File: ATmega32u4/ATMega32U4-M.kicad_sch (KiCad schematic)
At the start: 19 parts, among them U2 ATmega32U4-M, Y1 16MHz

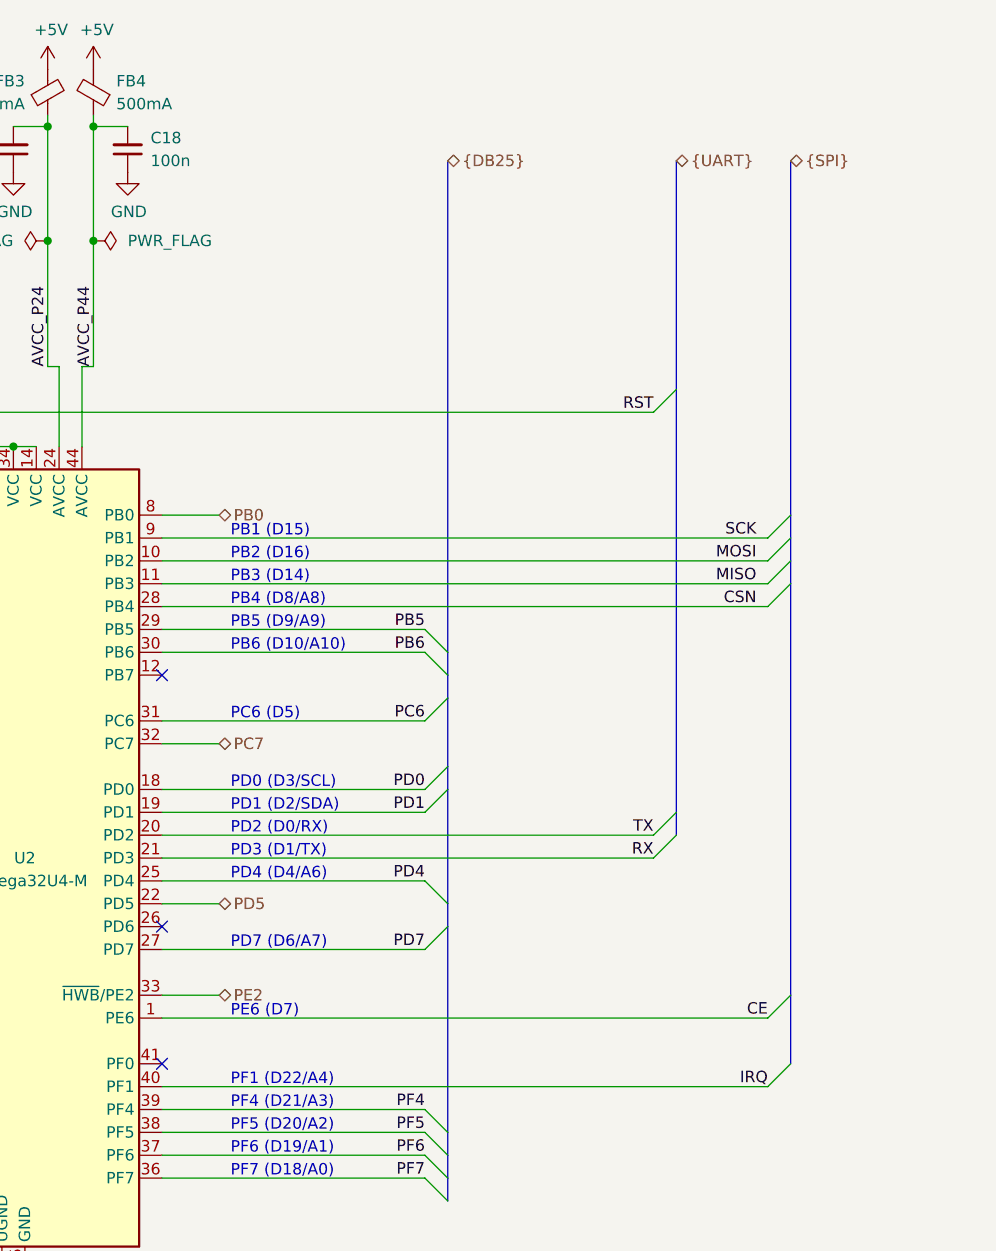
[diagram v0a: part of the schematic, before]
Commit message: Review and updates to power path
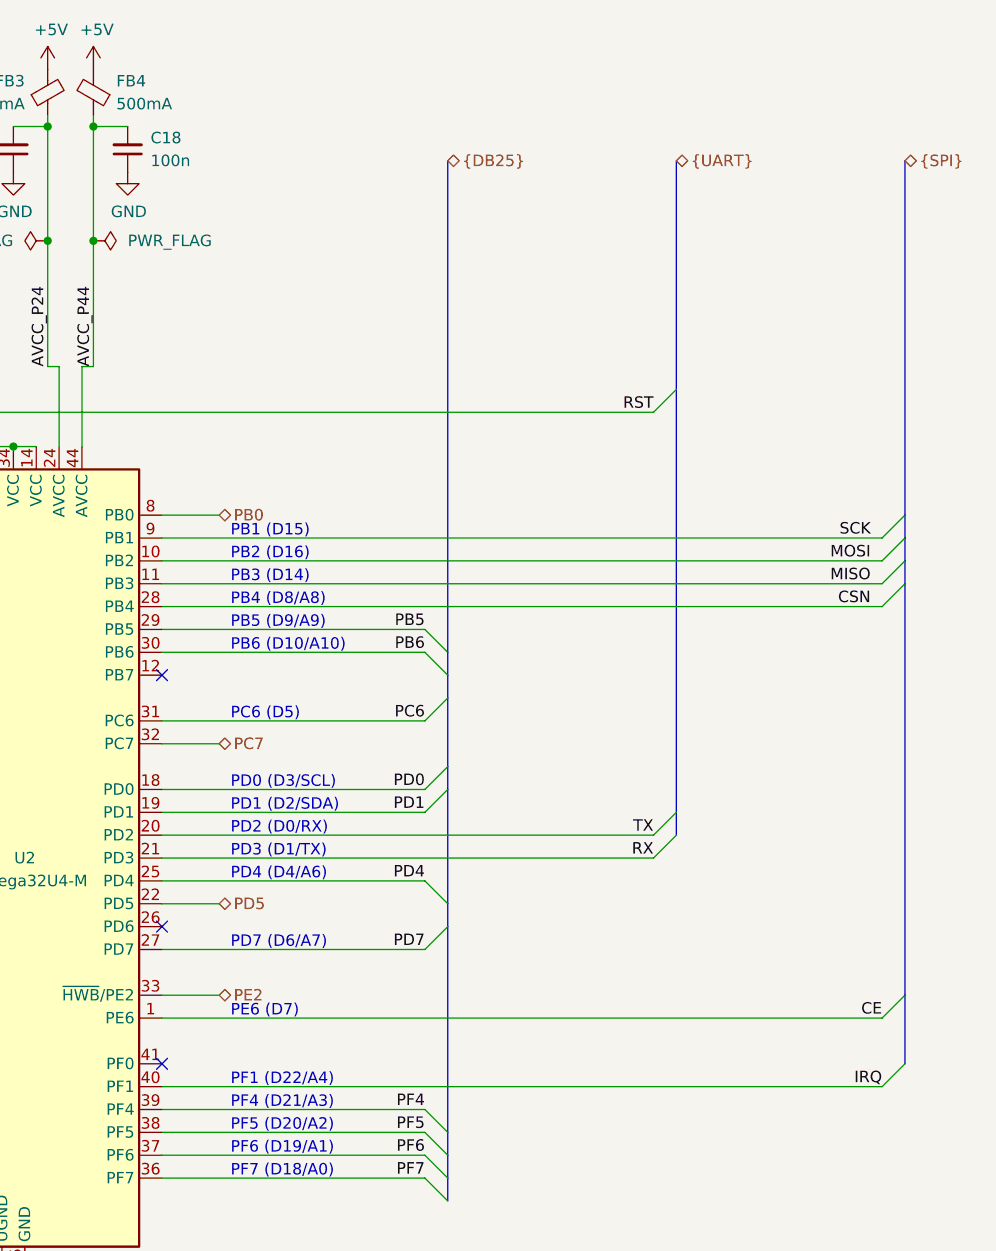
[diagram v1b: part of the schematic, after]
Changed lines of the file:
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@@
   (no_connect (at 120.65 138.43))
   (no_connect (at 90.17 92.71))
-  (bus_entry (at 187.96 80.01) (size 2.54 -2.54)
-    (stroke (width 0) (type default) (color 0 0 0 0))
-  )
-  (bus_entry (at 187.96 82.55) (size 2.54 -2.54)
+  (bus_entry (at 200.66 80.01) (size 2.54 -2.54)
+    (stroke (width 0) (type default) (color 0 0 0 0))
+  )
+  (bus_entry (at 200.66 82.55) (size 2.54 -2.54)
     (stroke (width 0) (type default) (color 0 0 0 0))
   )
@@
     (stroke (width 0) (type default) (color 0 0 0 0))
   )
-  (bus_entry (at 187.96 140.97) (size 2.54 -2.54)
+  (bus_entry (at 200.66 140.97) (size 2.54 -2.54)
     (stroke (width 0) (type default) (color 0 0 0 0))
   )
@@
     (stroke (width 0) (type default) (color 0 0 0 0))
   )
-  (bus_entry (at 187.96 87.63) (size 2.54 -2.54)
+  (bus_entry (at 200.66 87.63) (size 2.54 -2.54)
     (stroke (width 0) (type default) (color 0 0 0 0))
   )
@@
     (stroke (width 0) (type default) (color 0 0 0 0))
   )
-  (bus_entry (at 187.96 133.35) (size 2.54 -2.54)
+  (bus_entry (at 200.66 133.35) (size 2.54 -2.54)
     (stroke (width 0) (type default) (color 0 0 0 0))
   )
@@
     (stroke (width 0) (type default) (color 0 0 0 0))
   )
-  (bus_entry (at 187.96 85.09) (size 2.54 -2.54)
+  (bus_entry (at 200.66 85.09) (size 2.54 -2.54)
     (stroke (width 0) (type default) (color 0 0 0 0))
   )
@@
     (stroke (width 0) (type default) (color 0 0 0 0))
   )
-  (wire (pts (xy 120.65 80.01) (xy 187.96 80.01))
+  (wire (pts (xy 120.65 133.35) (xy 200.66 133.35))
+    (stroke (width 0) (type default) (color 0 0 0 0))
+  )
+  (wire (pts (xy 120.65 80.01) (xy 200.66 80.01))
     (stroke (width 0) (type default) (color 0 0 0 0))
   )
@@
     (stroke (width 0) (type default) (color 0 0 0 0))
   )
-  (wire (pts (xy 120.65 140.97) (xy 187.96 140.97))
-    (stroke (width 0) (type default) (color 0 0 0 0))
-  )
   (wire (pts (xy 120.65 143.51) (xy 149.86 143.51))
     (stroke (width 0) (type default) (color 0 0 0 0))
@@
     (stroke (width 0) (type default) (color 0 0 0 0))
   )
-  (bus (pts (xy 190.5 85.09) (xy 190.5 130.81))
+  (bus (pts (xy 203.2 85.09) (xy 203.2 130.81))
     (stroke (width 0) (type default) (color 0 0 0 0))
   )
@@
     (stroke (width 0) (type default) (color 0 0 0 0))
   )
+  (wire (pts (xy 120.65 140.97) (xy 200.66 140.97))
+    (stroke (width 0) (type default) (color 0 0 0 0))
+  )
   (wire (pts (xy 59.69 38.1) (xy 67.31 38.1))
     (stroke (width 0) (type default) (color 0 0 0 0))
   )
-  (bus (pts (xy 190.5 82.55) (xy 190.5 85.09))
+  (bus (pts (xy 203.2 82.55) (xy 203.2 85.09))
     (stroke (width 0) (type default) (color 0 0 0 0))
   )
@@
     (stroke (width 0) (type default) (color 0 0 0 0))
   )
-  (wire (pts (xy 120.65 85.09) (xy 187.96 85.09))
+  (wire (pts (xy 120.65 85.09) (xy 200.66 85.09))
     (stroke (width 0) (type default) (color 0 0 0 0))
   )
@@
     (stroke (width 0) (type default) (color 0 0 0 0))
   )
-  (bus (pts (xy 190.5 80.01) (xy 190.5 82.55))
+  (bus (pts (xy 203.2 80.01) (xy 203.2 82.55))
     (stroke (width 0) (type default) (color 0 0 0 0))
   )
@@
     (stroke (width 0) (type default) (color 0 0 0 0))
   )
-  (wire (pts (xy 120.65 133.35) (xy 187.96 133.35))
-    (stroke (width 0) (type default) (color 0 0 0 0))
-  )
   (bus (pts (xy 38.1 88.9) (xy 38.1 100.33))
     (stroke (width 0) (type default) (color 0 0 0 0))
@@
     (stroke (width 0) (type default) (color 0 0 0 0))
   )
-  (bus (pts (xy 190.5 130.81) (xy 190.5 138.43))
+  (bus (pts (xy 203.2 130.81) (xy 203.2 138.43))
     (stroke (width 0) (type default) (color 0 0 0 0))
   )
@@
     (stroke (width 0) (type default) (color 0 0 0 0))
   )
-  (wire (pts (xy 120.65 82.55) (xy 187.96 82.55))
+  (wire (pts (xy 120.65 82.55) (xy 200.66 82.55))
     (stroke (width 0) (type default) (color 0 0 0 0))
   )
@@
     (stroke (width 0) (type default) (color 0 0 0 0))
   )
-  (bus (pts (xy 190.5 77.47) (xy 190.5 80.01))
+  (bus (pts (xy 203.2 77.47) (xy 203.2 80.01))
     (stroke (width 0) (type default) (color 0 0 0 0))
   )
@@
     (stroke (width 0) (type default) (color 0 0 0 0))
   )
-  (bus (pts (xy 190.5 38.1) (xy 190.5 77.47))
-    (stroke (width 0) (type default) (color 0 0 0 0))
-  )
-  (wire (pts (xy 120.65 87.63) (xy 187.96 87.63))
+  (bus (pts (xy 203.2 38.1) (xy 203.2 77.47))
+    (stroke (width 0) (type default) (color 0 0 0 0))
+  )
+  (wire (pts (xy 120.65 87.63) (xy 200.66 87.63))
     (stroke (width 0) (type default) (color 0 0 0 0))
   )
@@
     (effects (font (size 1.27 1.27)) (justify right bottom))
   )
-  (label "CSN" (at 186.69 87.63 180)
+  (label "CSN" (at 199.39 87.63 180)
     (effects (font (size 1.27 1.27)) (justify right bottom))
   )
@@
     (effects (font (size 1.27 1.27)) (justify left bottom))
   )
-  (label "SCK" (at 186.69 80.01 180)
+  (label "SCK" (at 199.39 80.01 180)
     (effects (font (size 1.27 1.27)) (justify right bottom))
   )
@@
     (effects (font (size 1.27 1.27)) (justify left bottom))
   )
-  (label "CE" (at 187.96 133.35 180)
+  (label "CE" (at 200.66 133.35 180)
     (effects (font (size 1.27 1.27)) (justify right bottom))
   )
@@
     (effects (font (size 1.27 1.27)) (justify right bottom))
   )
-  (label "MISO" (at 186.69 85.09 180)
-    (effects (font (size 1.27 1.27)) (justify right bottom))
-  )
-  (label "IRQ" (at 187.96 140.97 180)
-    (effects (font (size 1.27 1.27)) (justify right bottom))
-  )
-  (label "MOSI" (at 186.69 82.55 180)
+  (label "MISO" (at 199.39 85.09 180)
+    (effects (font (size 1.27 1.27)) (justify right bottom))
+  )
+  (label "IRQ" (at 200.66 140.97 180)
+    (effects (font (size 1.27 1.27)) (justify right bottom))
+  )
+  (label "MOSI" (at 199.39 82.55 180)
     (effects (font (size 1.27 1.27)) (justify right bottom))
   )
@@
     (effects (font (size 1.27 1.27)) (justify left))
   )
-  (hierarchical_label "{SPI}" (shape bidirectional) (at 190.5 38.1 0)
+  (hierarchical_label "{SPI}" (shape bidirectional) (at 203.2 38.1 0)
     (effects (font (size 1.27 1.27)) (justify left))
   )

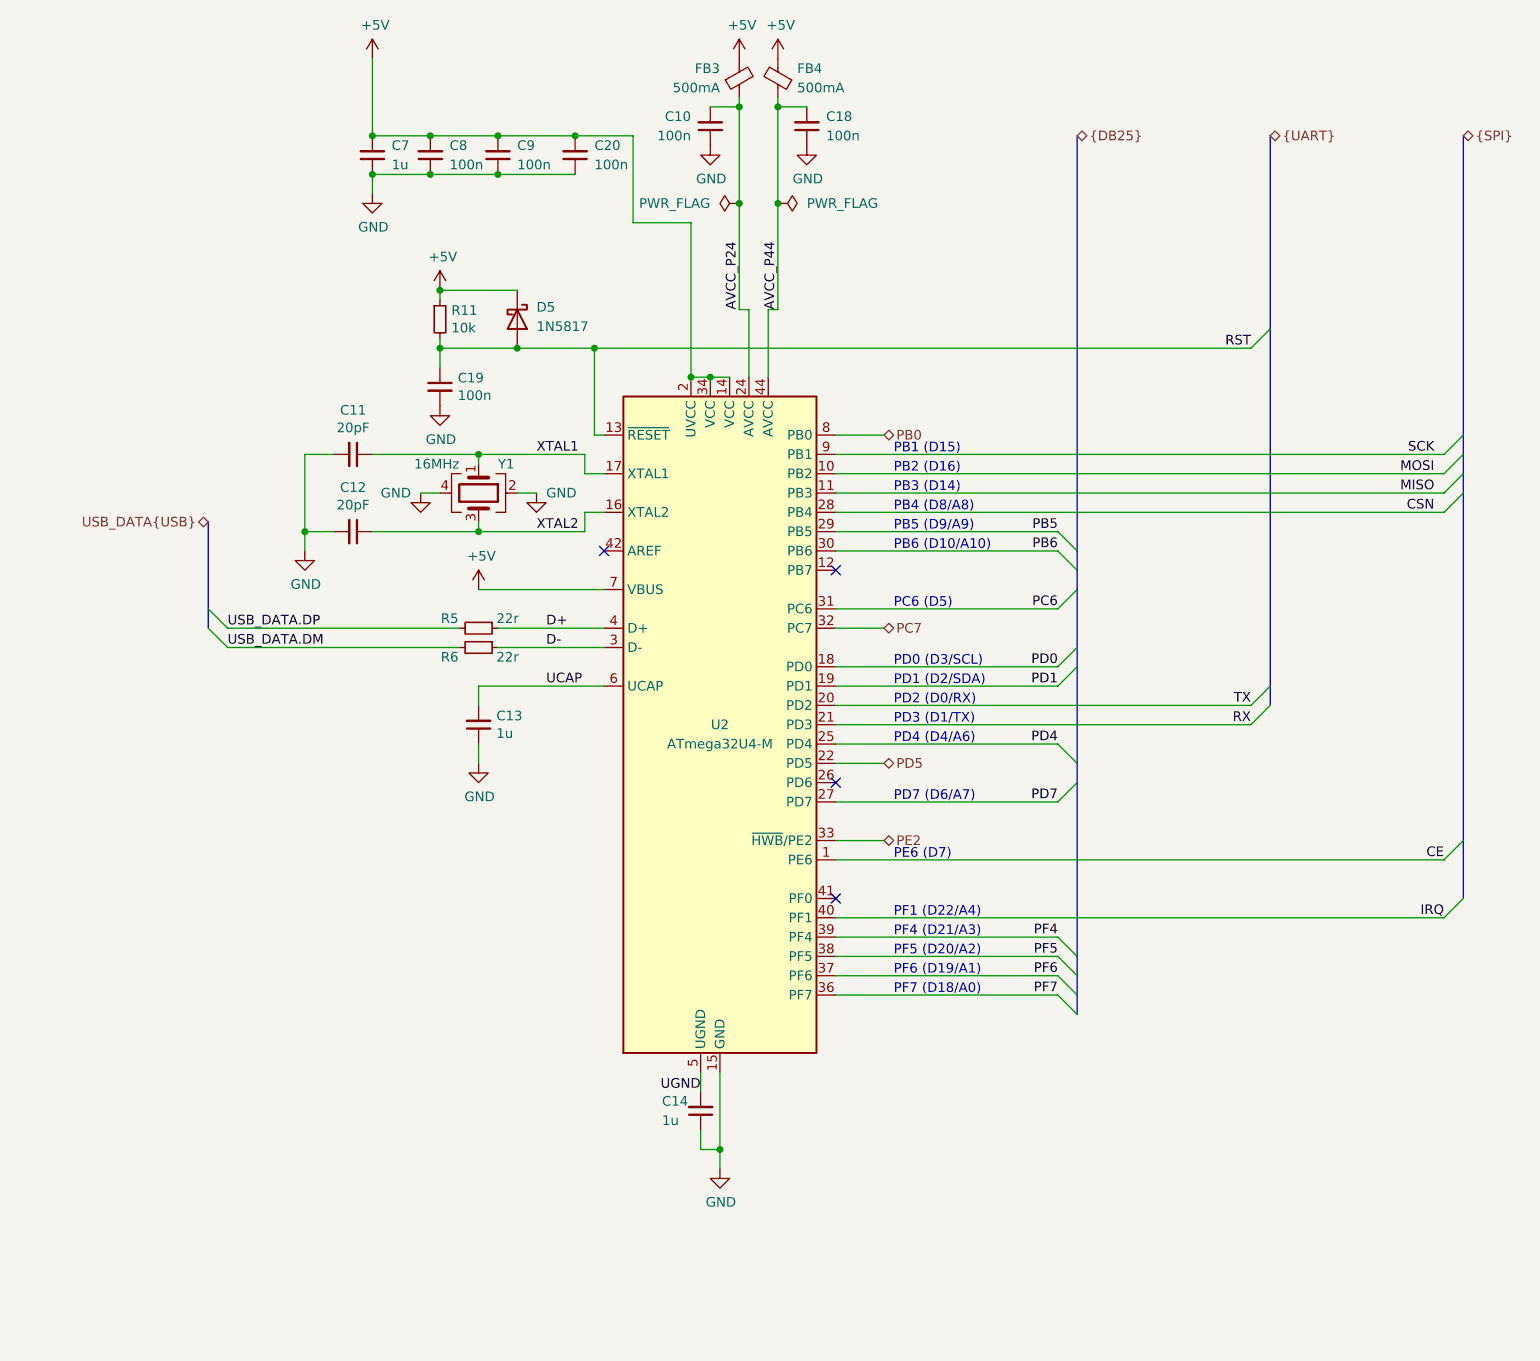
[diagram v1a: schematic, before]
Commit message: Schematic, routing and layout changes post review.
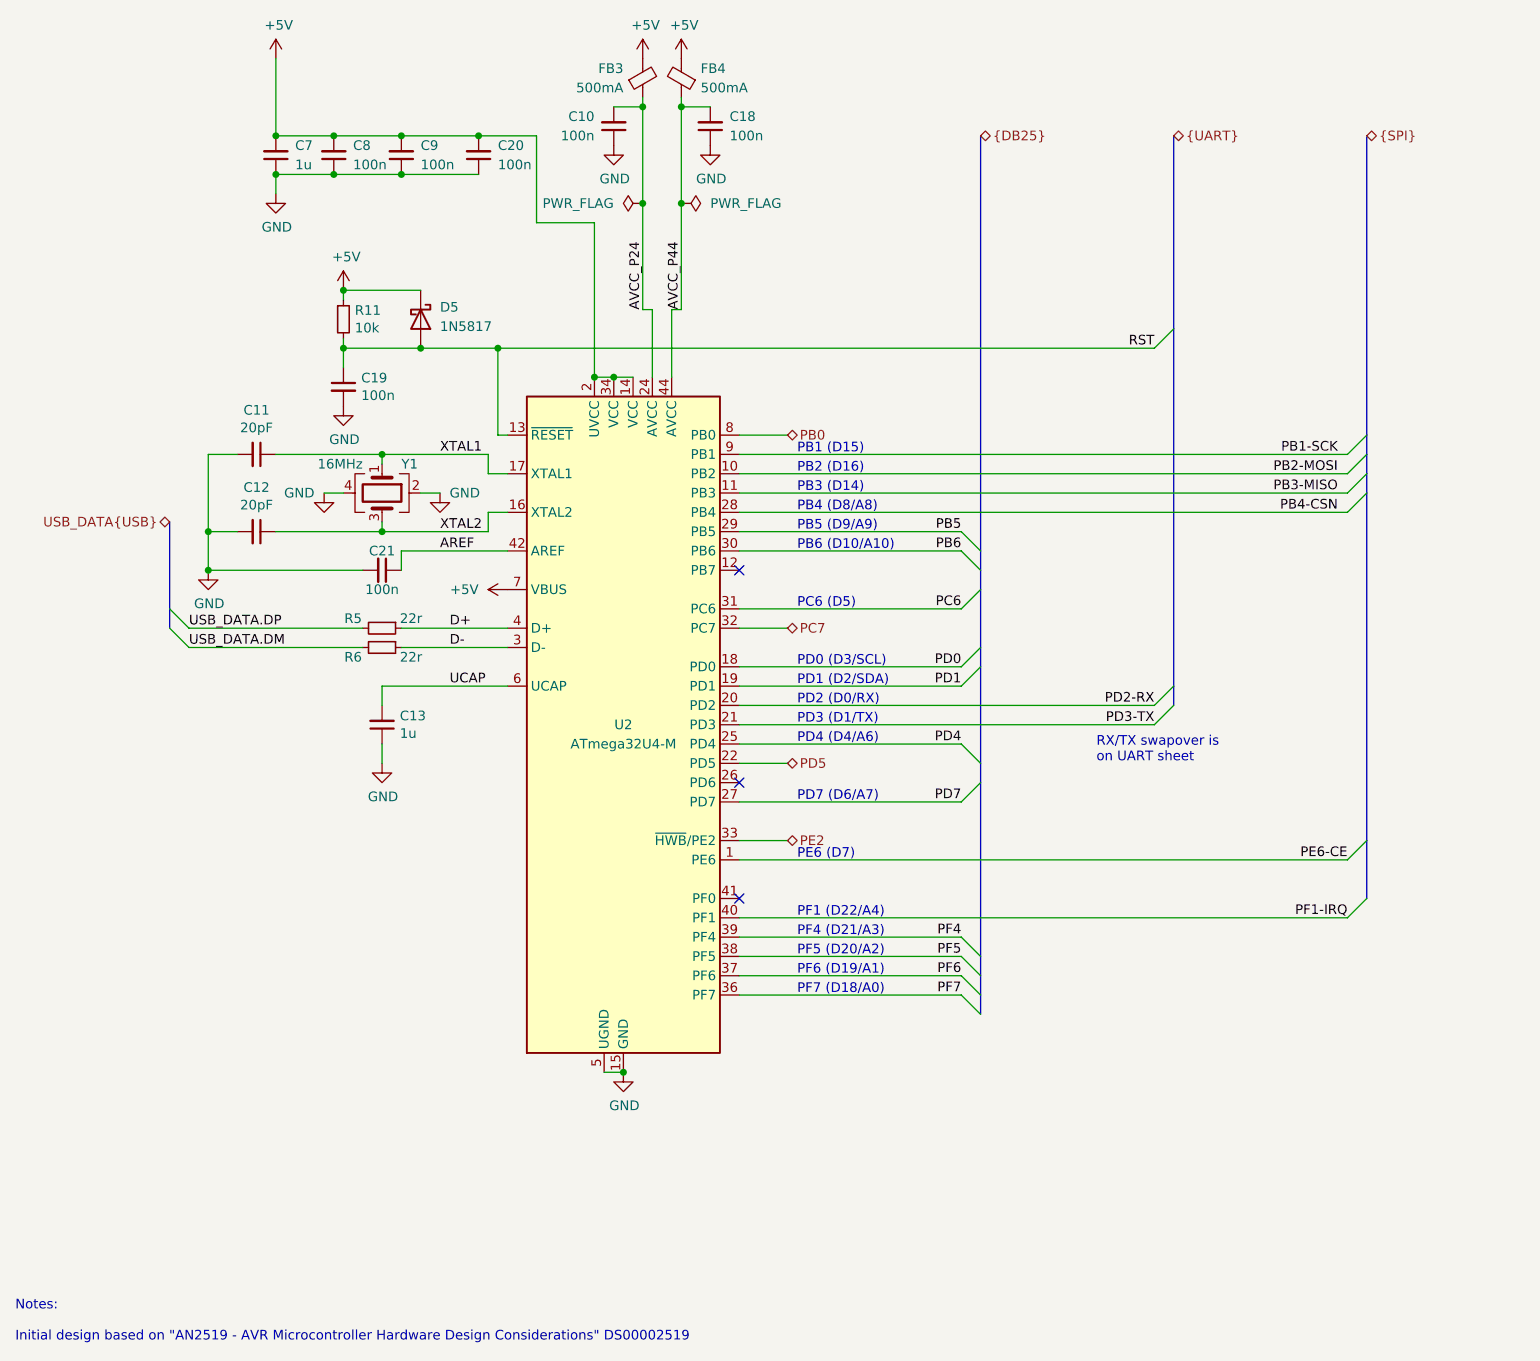
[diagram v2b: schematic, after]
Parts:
- removed C14: 1u, Capacitor_SMD:C_0603_1608Metric, symbol Device:C_Small
- added C21: 100n, Capacitor_SMD:C_0603_1608Metric, symbol Device:C_Small
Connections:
- net UGND is gone; now on net GND: U2.5 (UGND)
- net GND: now also C21.2
- net AREF: now reaches U2.42 (AREF)
- net AREF: now also C21.1
- net CE renamed PE6-CE
- net CSN renamed PB4-CSN
- net IRQ renamed PF1-IRQ
- net MISO renamed PB3-MISO
- net MOSI renamed PB2-MOSI
- net RX renamed PD3-TX
- net SCK renamed PB1-SCK
- net TX renamed PD2-RX
- no-connect marks 4 -> 3
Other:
- note added: "Notes: Initial design based on "AN2519 - AVR Microcontroller Hardware Design Considerations" DS00002519"
- note added: "RX/TX swapover is on UART sheet"
- moved on the sheet: C10, C11, C12, C13, C18, C19, C20, C7, C8, C9, D5, FB3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
